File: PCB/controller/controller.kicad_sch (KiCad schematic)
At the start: 32 parts, among them J1 USB_C_Receptacle_USB2.0_16P, Q5 BSS138, SW2 SW_Push, SW3 SW_Push, U1 NanoS3, U2 COM-09032, U3 TPS61200DRC

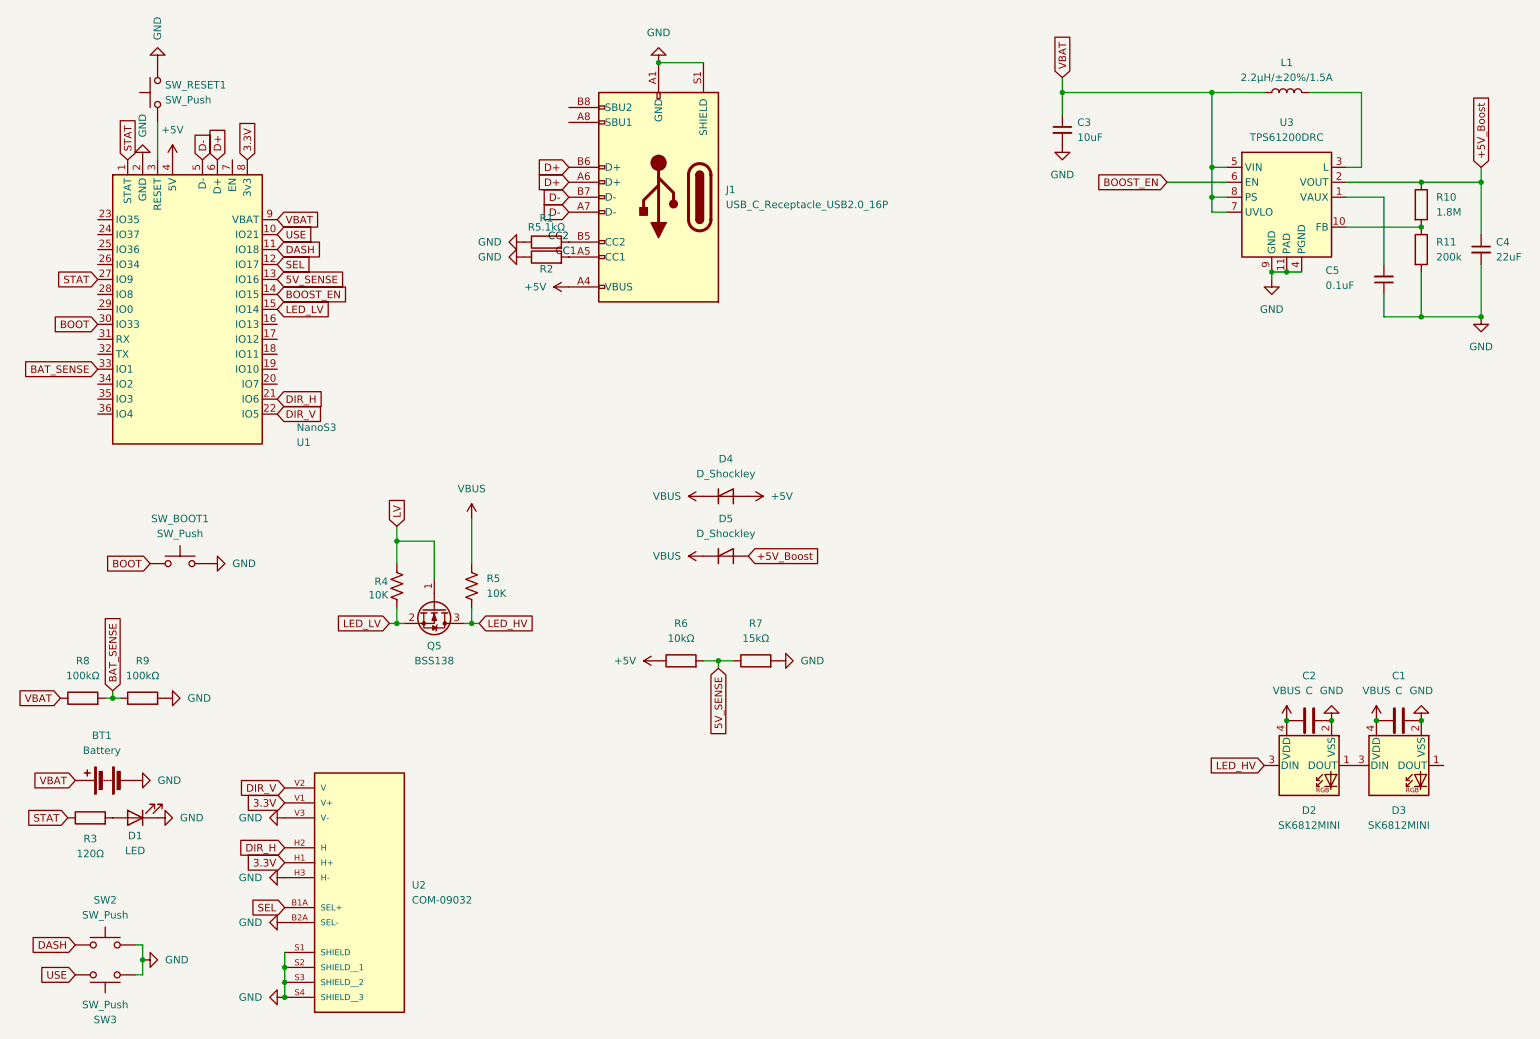
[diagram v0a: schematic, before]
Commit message: Add production files for PCB controller design
- Created designators.csv with component designators and their counts.
- Added netlist.ipc containing detailed netlist information for PCB connections.
- Introduced positions.csv to specify component positions, rotations, and layers on the PCB.
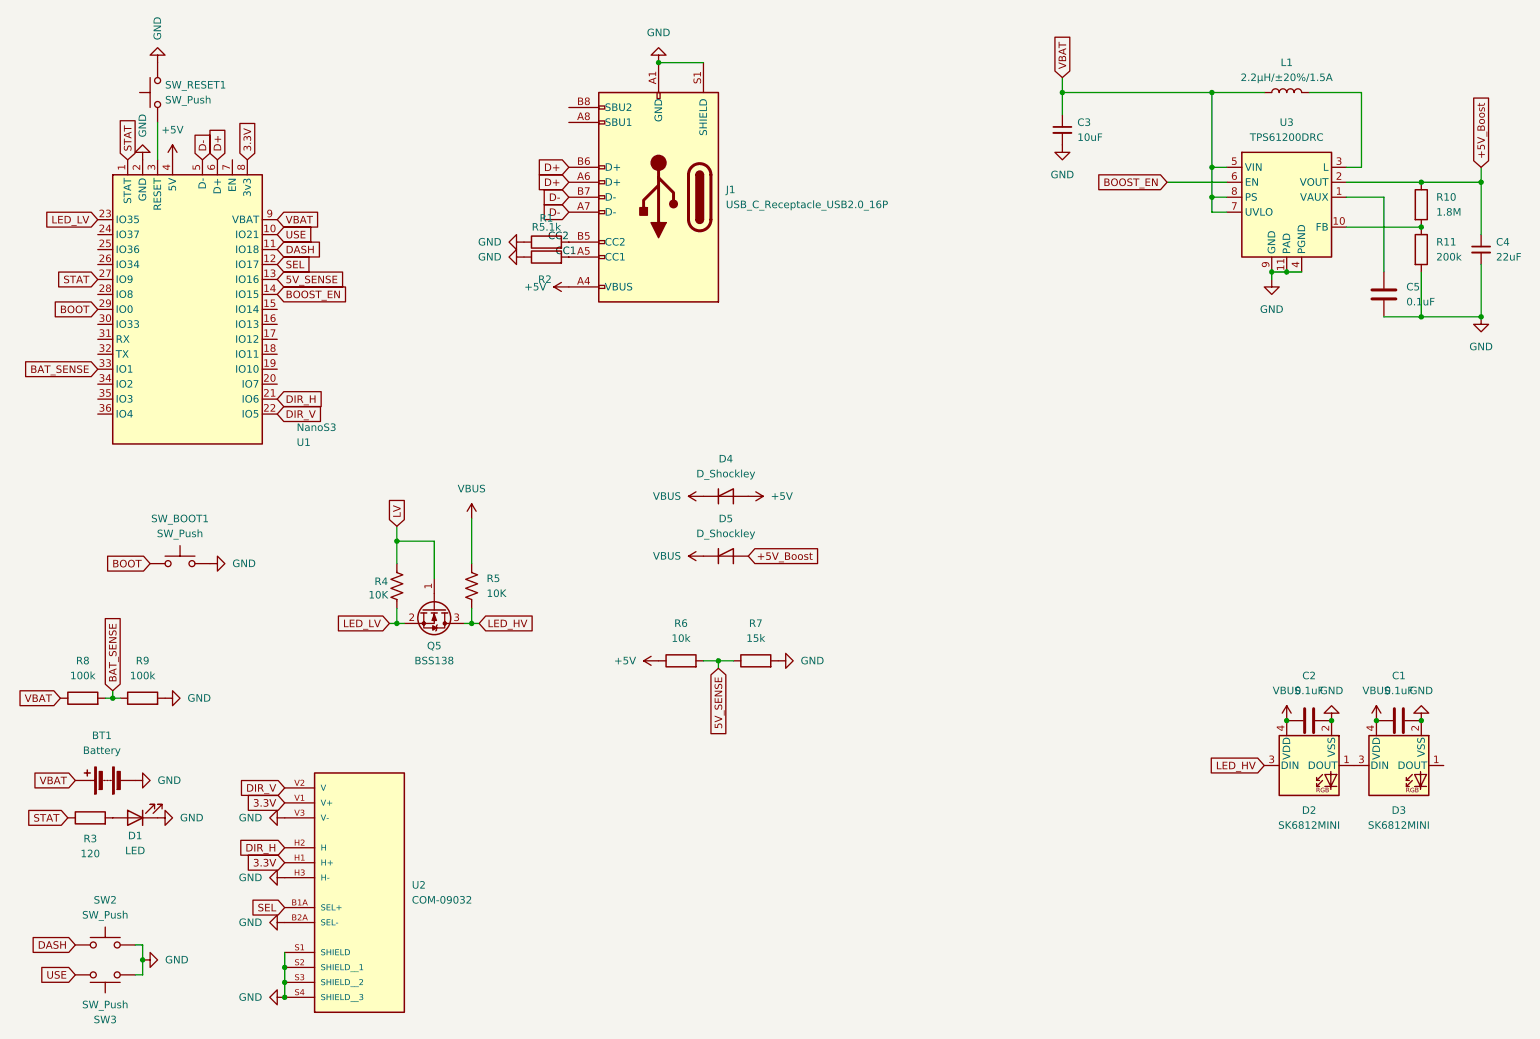
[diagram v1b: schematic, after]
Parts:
- removed C5: 0.1uF, Capacitor_SMD:C_0603_1608Metric_Pad1.08x0.95mm_HandSolder, symbol Device:C_Small
- added C5: 0.1uF, Capacitor_SMD:C_0805_2012Metric_Pad1.18x1.45mm_HandSolder, symbol Device:C
- C1, C2: value C -> 0.1uF
- R1, R2: value R5.1kΩ -> R5.1k
- R3: value 120Ω -> 120
- R6: value 10kΩ -> 10k
- R7: value 15kΩ -> 15k
- R8, R9: value 100kΩ -> 100k
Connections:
- net BOOT: now also U1.29 (IO0); no longer U1.30 (IO33)
- net GND: now also C5.1
- net LED_LV: now also U1.23 (IO35); no longer U1.15 (IO14)
- net at U3.1 (VAUX): now also C5.2
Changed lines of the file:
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@@
 	(wire
 		(pts
-			(xy 240.03 46.99) (xy 246.38 46.99)
+			(xy 246.38 46.99) (xy 246.38 59.69)
 		)
 		(stroke
@@
 	(wire
 		(pts
-			(xy 123.19 24.13) (xy 130.81 24.13)
+			(xy 240.03 46.99) (xy 246.38 46.99)
 		)
 		(stroke
@@
 	(wire
 		(pts
-			(xy 246.38 63.5) (xy 246.38 67.31)
+			(xy 123.19 24.13) (xy 130.81 24.13)
 		)
 		(stroke
@@
 	(wire
 		(pts
-			(xy 246.38 46.99) (xy 246.38 58.42)
-		)
-		(stroke
-			(width 0)
-			(type default)
-		)
-	)
-	(wire
-		(pts
 			(xy 91.44 119.38) (xy 90.17 119.38)
 		)
@@
 		)
 	)
+	(global_label "BOOT"
+		(shape input)
+		(at 27.94 66.04 180)
+		(fields_autoplaced yes)
+		(effects
+			(font
+				(size 1.27 1.27)
+			)
+			(justify right)
+		)
+		(property "Intersheetrefs" "${INTERSHEET_REFS}"
+			(at 20.0562 66.04 0)
+			(effects
+				(font
+					(size 1.27 1.27)
+				)
+				(justify right)
+				(hide yes)
+			)
+		)
+	)
 	(global_label "D+"
 		(shape input)
@@
 		)
 	)
-	(global_label "SEL"
+	(global_label "LED_LV"
 		(shape input)
-		(at 59.69 167.64 180)
+		(at 27.94 50.8 180)
 		(fields_autoplaced yes)
 		(effects
@@
 		)
 		(property "Intersheetrefs" "${INTERSHEET_REFS}"
-			(at 53.3182 167.64 0)
+			(at 18.4234 50.8 0)
 			(effects
 				(font
@@
 		)
 	)
-	(global_label "BOOT"
+	(global_label "SEL"
 		(shape input)
-		(at 27.94 68.58 180)
+		(at 59.69 167.64 180)
 		(fields_autoplaced yes)
 		(effects
@@
 		)
 		(property "Intersheetrefs" "${INTERSHEET_REFS}"
-			(at 20.0562 68.58 0)
+			(at 53.3182 167.64 0)
 			(effects
 				(font
@@
 		)
 	)
-	(global_label "LED_LV"
-		(shape input)
-		(at 58.42 66.04 0)
-		(fields_autoplaced yes)
-		(effects
-			(font
-				(size 1.27 1.27)
-			)
-			(justify left)
-		)
-		(property "Intersheetrefs" "${INTERSHEET_REFS}"
-			(at 67.9366 66.04 0)
-			(effects
-				(font
-					(size 1.27 1.27)
-				)
-				(justify left)
-				(hide yes)
-			)
-		)
-	)
 	(global_label "DIR_V"
 		(shape input)
@@
 			)
 		)
-		(property "Value" "15kΩ"
+		(property "Value" "15k"
 			(at 139.7 121.92 90)
 			(effects
@@
 		(dnp no)
 		(property "Reference" "R2"
-			(at 104.14 59.182 90)
+			(at 103.886 60.96 90)
 			(effects
 				(font
@@
 			)
 		)
-		(property "Value" "R5.1kΩ"
+		(property "Value" "R5.1k"
 			(at 104.14 60.706 90)
 			(effects
@@
 			)
 		)
-		(property "Value" "R5.1kΩ"
+		(property "Value" "R5.1k"
 			(at 104.14 52.07 90)
 			(effects
@@
 	)
 	(symbol
+		(lib_id "Device:C")
+		(at 246.38 63.5 180)
+		(unit 1)
+		(exclude_from_sim no)
+		(in_bom yes)
+		(on_board yes)
+		(dnp no)
+		(fields_autoplaced yes)
+		(property "Reference" "C5"
+			(at 250.19 62.2299 0)
+			(effects
+				(font
+					(size 1.27 1.27)
+				)
+				(justify right)
+			)
+		)
+		(property "Value" "0.1uF"
+			(at 250.19 64.7699 0)
+			(effects
+				(font
+					(size 1.27 1.27)
+				)
+				(justify right)
+			)
+		)
+		(property "Footprint" "Capacitor_SMD:C_0805_2012Metric_Pad1.18x1.45mm_HandSolder"
+			(at 245.4148 59.69 0)
+			(effects
+				(font
+					(size 1.27 1.27)
+				)
+				(hide yes)
+			)
+		)
+		(property "Datasheet" "~"
+			(at 246.38 63.5 0)
+			(effects
+				(font
+					(size 1.27 1.27)
+				)
+				(hide yes)
+			)
+		)
+		(property "Description" "Unpolarized capacitor"
+			(at 246.38 63.5 0)
+			(effects
+				(font
+					(size 1.27 1.27)
+				)
+				(hide yes)
+			)
+		)
+		(pin "2"
+		)
+		(pin "1"
+		)
+		(instances
+			(project "controller"
+				(path "/ce012b05-d66b-413a-8b7d-ace79b999db0"
+					(reference "C5")
+					(unit 1)
+				)
+			)
+		)
+	)
+	(symbol
 		(lib_id "power:VBUS")
 		(at 130.81 107.95 90)
@@
 			)
 		)
-		(property "Value" "100kΩ"
+		(property "Value" "100k"
 			(at 35.56 128.27 90)
 			(effects
@@
 			)
 		)
-		(property "Value" "10kΩ"
+		(property "Value" "10k"
 			(at 127 121.92 90)
 			(effects
@@
 			)
 		)
-		(property "Value" "100kΩ"
+		(property "Value" "100k"
 			(at 25.4 128.27 90)
 			(effects
@@
 	)
 	(symbol
-		(lib_id "Device:C_Small")
-		(at 246.38 60.96 180)
-		(unit 1)
-		(exclude_from_sim no)
-		(in_bom yes)
-		(on_board yes)
-		(dnp no)
-		(property "Reference" "C5"
-			(at 236.474 59.436 0)
-			(effects
-				(font
-					(size 1.27 1.27)
-				)
-				(justify right)
-			)
-		)
-		(property "Value" "0.1uF"
-			(at 236.474 61.976 0)
-			(effects
-				(font
-					(size 1.27 1.27)
-				)
-				(justify right)
-			)
-		)
-		(property "Footprint" "Capacitor_SMD:C_0603_1608Metric_Pad1.08x0.95mm_HandSolder"
-			(at 246.38 60.96 0)
-			(effects
-				(font
-					(size 1.27 1.27)
-				)
-				(hide yes)
-			)
-		)
-		(property "Datasheet" "~"
-			(at 246.38 60.96 0)
-			(effects
-				(font
-					(size 1.27 1.27)
-				)
-				(hide yes)
-			)
-		)
-		(property "Description" "Unpolarized capacitor, small symbol"
-			(at 246.38 60.96 0)
-			(effects
-				(font
-					(size 1.27 1.27)
-				)
-				(hide yes)
-			)
-		)
-		(pin "2"
-		)
-		(pin "1"
-		)
-		(instances
-			(project "controller"
-				(path "/ce012b05-d66b-413a-8b7d-ace79b999db0"
-					(reference "C5")
-					(unit 1)
-				)
-			)
-		)
-	)
-	(symbol
 		(lib_id "power:GND")
 		(at 35.56 176.53 90)
@@
 			)
 		)
-		(property "Value" "C"
+		(property "Value" "0.1uF"
 			(at 248.92 130.81 90)
 			(effects
@@
 			)
 		)
-		(property "Value" "C"
+		(property "Value" "0.1uF"
 			(at 233.68 130.81 90)
 			(effects
@@
 			)
 		)
-		(property "Value" "120Ω"
+		(property "Value" "120"
 			(at 26.67 158.496 90)
 			(effects

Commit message: Add lock file for PCB controller with hostname and username information
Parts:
- C5: footprint Capacitor_SMD:C_0805_2012Metric_Pad1.18x1.45mm_HandSolder -> Capacitor_SMD:C_0603_1608Metric_Pad1.08x0.95mm_HandSolder
- J1: footprint Connector_USB:USB_C_Receptacle_XKB_U262-16XN-4BVC11 -> Connector_USB:USB_C_Receptacle_G-Switch_GT-USB-7010ASV
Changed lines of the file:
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@@
 			)
 		)
-		(property "Footprint" "Capacitor_SMD:C_0805_2012Metric_Pad1.18x1.45mm_HandSolder"
+		(property "Footprint" "Capacitor_SMD:C_0603_1608Metric_Pad1.08x0.95mm_HandSolder"
 			(at 245.4148 59.69 0)
 			(effects
@@
 			)
 		)
-		(property "Footprint" "Connector_USB:USB_C_Receptacle_XKB_U262-16XN-4BVC11"
+		(property "Footprint" "Connector_USB:USB_C_Receptacle_G-Switch_GT-USB-7010ASV"
 			(at 119.38 46.99 0)
 			(effects

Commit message: firmware
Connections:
- net 3.3V: now also C3.1, L1.1, U3.5 (VIN), U3.7 (UVLO), U3.8 (PS)
- net VBAT: no longer C3.1, L1.1, U3.5 (VIN), U3.7 (UVLO), U3.8 (PS)
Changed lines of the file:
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@@
 		)
 	)
-	(global_label "VBAT"
+	(global_label "3.3V"
 		(shape input)
 		(at 191.77 26.67 90)
@@
 		)
 		(property "Intersheetrefs" "${INTERSHEET_REFS}"
-			(at 191.77 19.27 90)
+			(at 191.77 19.5724 90)
 			(effects
 				(font
